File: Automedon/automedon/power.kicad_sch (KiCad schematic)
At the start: 22 parts, among them J29 3211771, J30 3211771, J31 3211771, J32 3211771, J33 3211771, J34 3211771, J35 3211771, J36 3211771, J37 3211771, J38 3211771, J39 3211771, J40 3211771, J41 3211771, J42 3211771, J43 3211771, J44 3211771

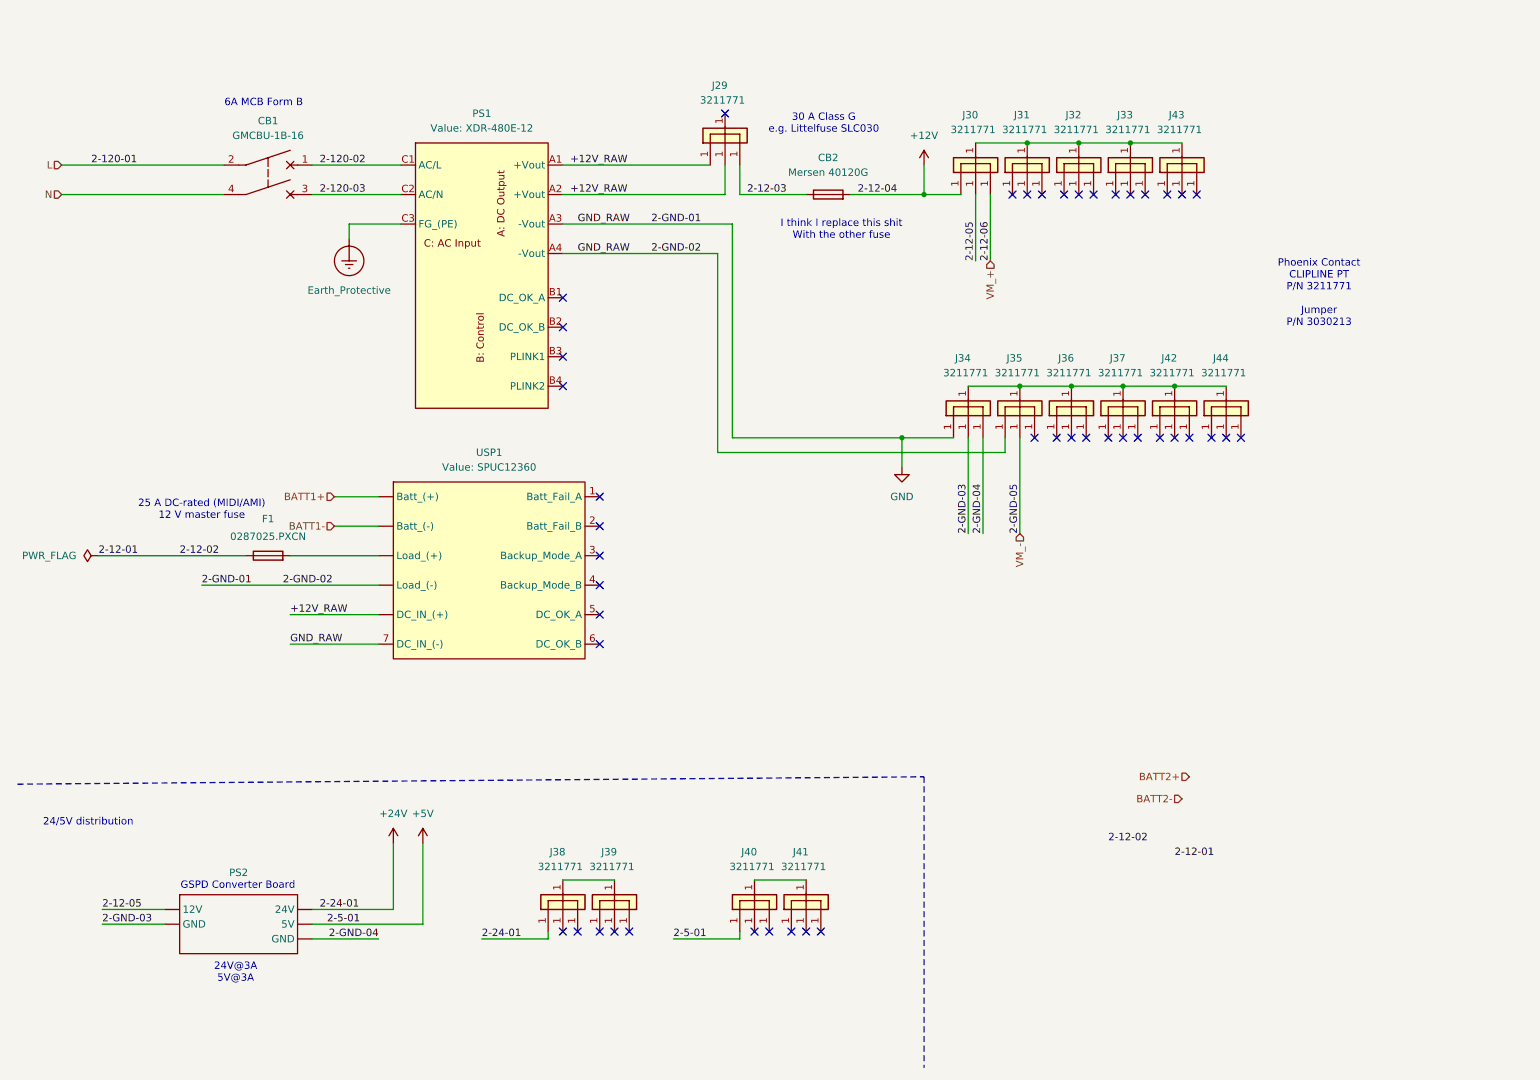
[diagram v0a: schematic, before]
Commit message: Updated schematics and symbols based on feedback
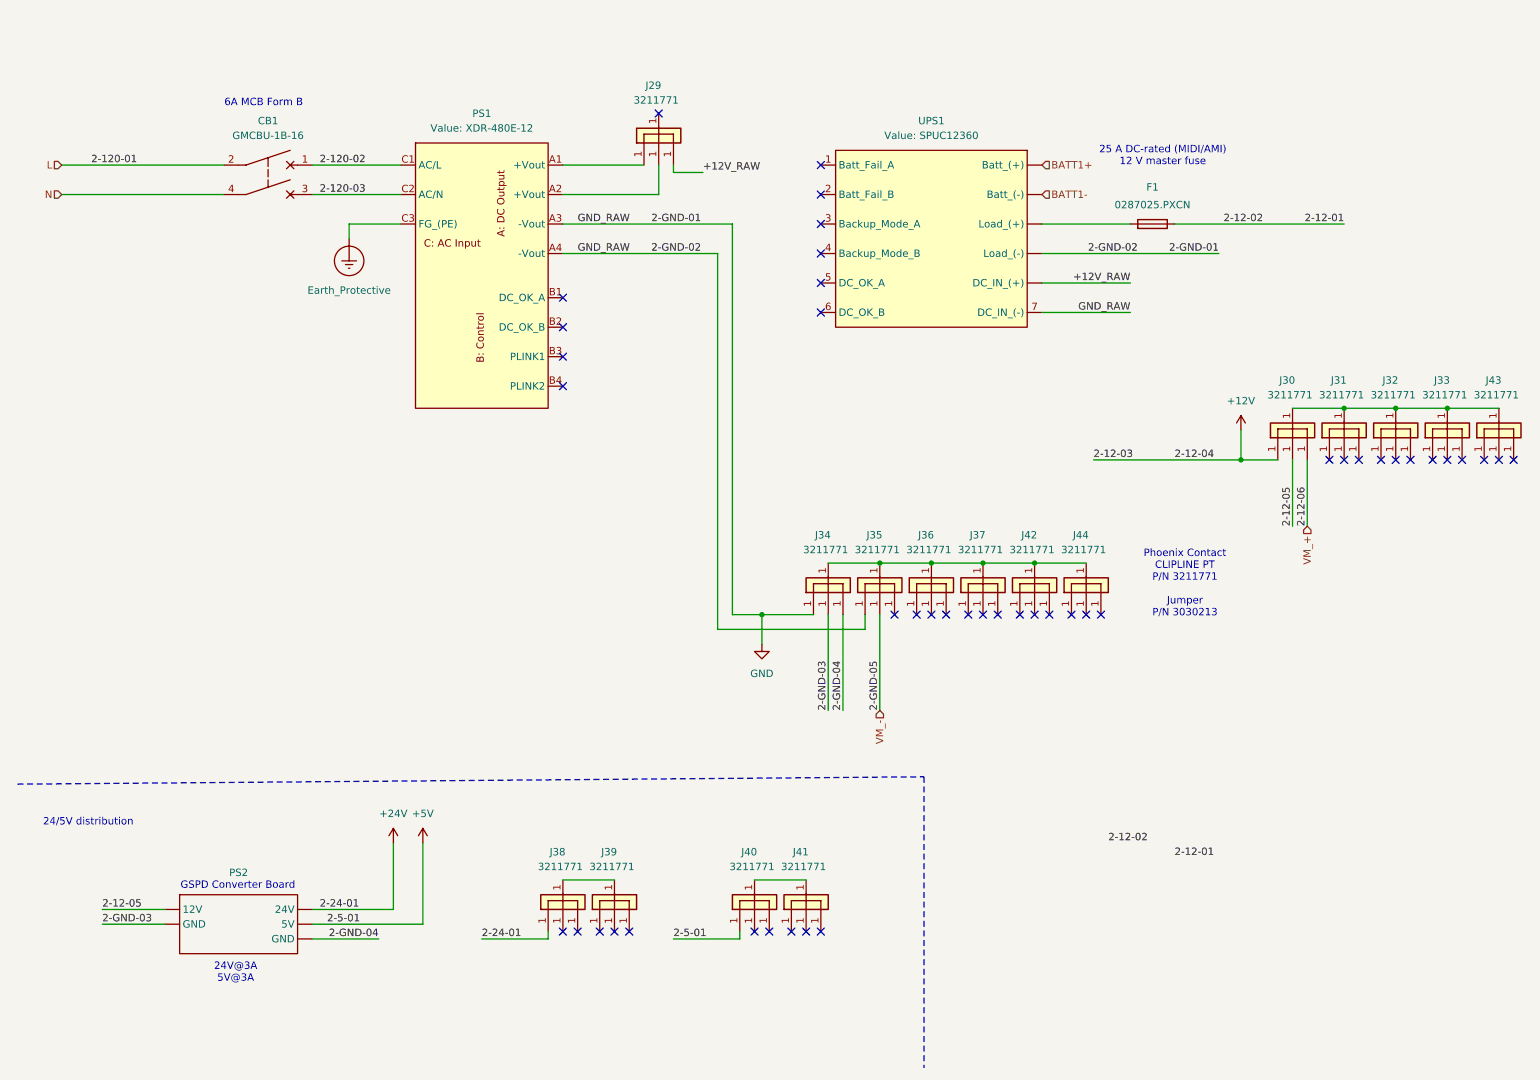
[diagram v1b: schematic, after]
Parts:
- removed CB2: Mersen 40120G, symbol Device:Fuse
- renumbered USP1 to UPS1
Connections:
- net 2-12-03 is gone; now on net +12V_RAW: J29.1
- net +12V_RAW: no longer PS1.A1 (+Vout), PS1.A2 (+Vout)
- net at J37.1: now also J34.1, J35.1, J36.1, J42.1, J44.1
- net at J39.1: no longer J38.1
- net at J41.1: now also J40.1
- new net: J30.1, J31.1, J32.1, J33.1, J43.1
- new net: J29.1, PS1.A1 (+Vout)
- new net: J29.1, PS1.A2 (+Vout)
- new net: J38.1, J39.1
- now unconnected: J31.1, J32.1, J33.1, J36.1, J42.1, J43.1, J44.1
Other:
- note removed: "30 A Class G e.g. Littelfuse SLC030"
- note removed: "I think I replace this shit With the other fuse"
- moved on the sheet: F1, J29, J30, J31, J32, J33, J34, J35, J36, J37, J42, J43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

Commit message: Update power schematic (power.kicad_sch)
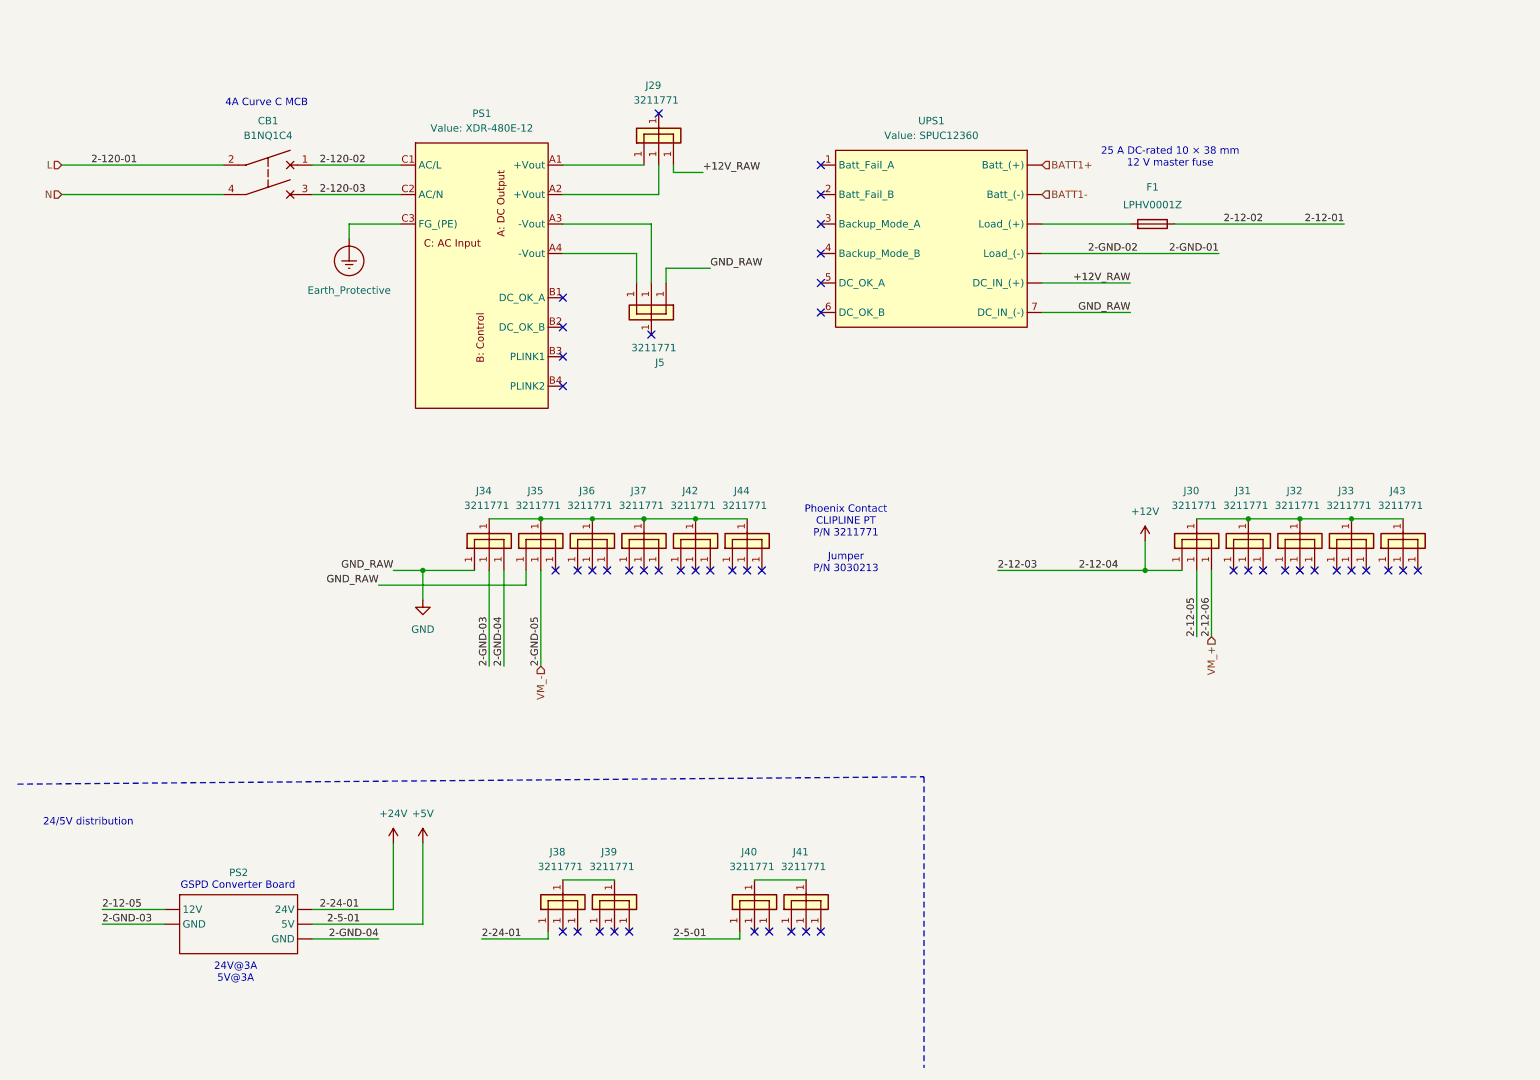
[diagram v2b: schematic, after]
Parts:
- added J5: 3211771, symbol automedon:CONN_TERM_3
- CB1: value GMCBU-1B-16 -> B1NQ1C4
- F1: value 0287025.PXCN -> LPHV0001Z
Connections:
- net GND: now also J5.1; no longer PS1.A3 (-Vout), PS1.A4 (-Vout), UPS1. (DC_IN_(+))
- net at J37.1: now also J34.1, J35.1, J36.1, J42.1, J44.1
- net at J39.1: no longer J38.1
- net at J41.1: now also J40.1
- new net: J30.1, J31.1, J32.1, J33.1, J43.1
- new net: J5.1, PS1.A3 (-Vout)
- new net: J5.1, PS1.A4 (-Vout)
- new net: J38.1, J39.1
- new net 2-GND-01: UPS1. (DC_IN_(+))
- now unconnected: J31.1, J32.1, J33.1, J36.1, J42.1, J43.1, J44.1
- no-connect marks 46 -> 47
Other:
- note added: "25 A DC-rated 10 × 38 mm 12 V master fuse"
- note added: "4A Curve C MCB"
- note removed: "25 A DC-rated (MIDI/AMI) 12 V master fuse"
- note removed: "6A MCB Form B"
- moved on the sheet: J30, J31, J32, J33, J34, J35, J36, J37, J42, J43, J44

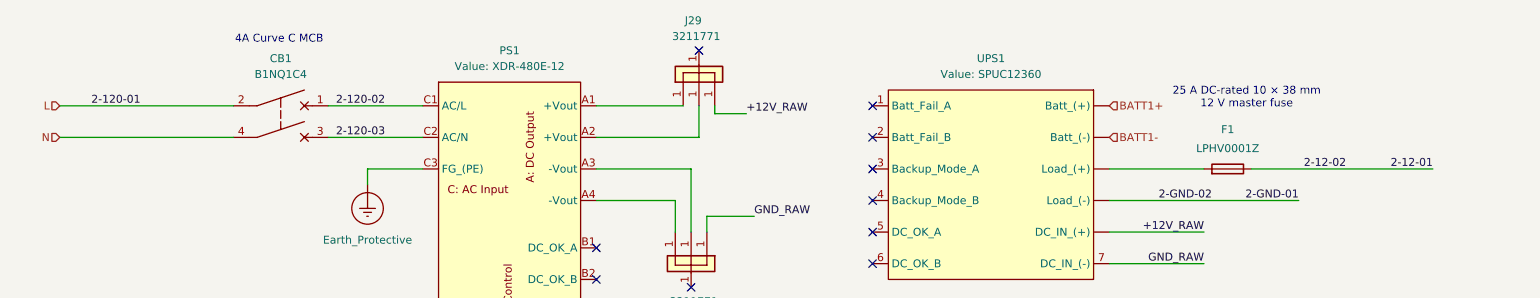
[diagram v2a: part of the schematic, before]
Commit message: updated cb1 and f1 on schematic
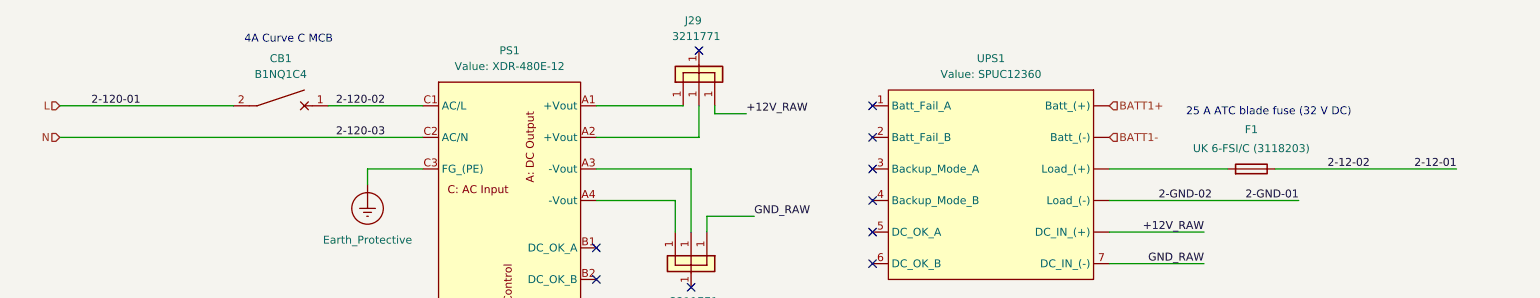
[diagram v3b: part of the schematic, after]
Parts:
- removed CB1: B1NQ1C4, symbol Device:CircuitBreaker_2P
- added CB1: B1NQ1C4, symbol Device:CircuitBreaker_1P
- F1: value LPHV0001Z -> UK 6-FSI/C (3118203)
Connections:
- net 2-120-03 is gone; now on net N: PS1.C2 (AC/N)
- net 2-120-02: now also CB1.1
- net L: now also CB1.2
- net at J37.1: now also J34.1, J35.1, J36.1, J42.1, J44.1
- net at J39.1: no longer J38.1
- net at J41.1: now also J40.1
- new net: J30.1, J31.1, J32.1, J33.1, J43.1
- new net: J38.1, J39.1
- now unconnected: J31.1, J32.1, J33.1, J36.1, J42.1, J43.1, J44.1
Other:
- note added: "25 A ATC blade fuse (32 V DC)"
- note removed: "25 A DC-rated 10 × 38 mm 12 V master fuse"
- moved on the sheet: F1
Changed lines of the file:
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@@
 	(generator_version "9.0")
 	(paper "A4")
-	(text "25 A DC-rated 10 × 38 mm\n12 V master fuse\n"
-		(exclude_from_sim no)
-		(at 211.328 40.64 0)
+	(text "25 A ATC blade fuse (32 V DC)"
+		(exclude_from_sim no)
+		(at 214.884 42.926 0)
 		(effects
 			(font
@@
 	(text "4A Curve C MCB"
 		(exclude_from_sim no)
-		(at 55.626 31.242 0)
+		(at 57.15 31.242 0)
 		(effects
 			(font
@@
 	(wire
 		(pts
-			(xy 20.32 46.99) (xy 48.26 46.99)
+			(xy 20.32 46.99) (xy 78.74 46.99)
 		)
 		(stroke
@@
 	(wire
 		(pts
-			(xy 241.3 52.07) (xy 212.09 52.07)
+			(xy 245.11 52.07) (xy 215.9 52.07)
 		)
 		(stroke
@@
 	(wire
 		(pts
-			(xy 63.5 46.99) (xy 78.74 46.99)
-		)
-		(stroke
-			(width 0)
-			(type default)
-		)
-	)
-	(wire
-		(pts
-			(xy 204.47 52.07) (xy 189.23 52.07)
+			(xy 208.28 52.07) (xy 189.23 52.07)
 		)
 		(stroke
@@
 	)
 	(label "2-12-02"
-		(at 227.33 52.07 180)
+		(at 231.14 52.07 180)
 		(effects
 			(font
@@
 	)
 	(label "2-12-01"
-		(at 241.3 52.07 180)
+		(at 245.11 52.07 180)
 		(effects
 			(font
@@
 	(symbol
 		(lib_id "Device:Fuse")
-		(at 208.28 52.07 270)
+		(at 212.09 52.07 270)
 		(mirror x)
 		(unit 1)
@@
 		(dnp no)
 		(property "Reference" "F1"
-			(at 208.28 45.72 90)
-			(effects
-				(font
-					(size 1.27 1.27)
-				)
-			)
-		)
-		(property "Value" "LPHV0001Z"
-			(at 208.28 48.768 90)
+			(at 212.09 45.72 90)
+			(effects
+				(font
+					(size 1.27 1.27)
+				)
+			)
+		)
+		(property "Value" "UK 6-FSI/C (3118203)"
+			(at 212.09 48.768 90)
 			(effects
 				(font
@@
 		)
 		(property "Footprint" ""
-			(at 208.28 53.848 90)
+			(at 212.09 53.848 90)
 			(effects
 				(font
@@
 		)
 		(property "Datasheet" "~"
-			(at 208.28 52.07 0)
+			(at 212.09 52.07 0)
 			(effects
 				(font
@@
 		)
 		(property "Description" "Fuse"
-			(at 208.28 52.07 0)
+			(at 212.09 52.07 0)
 			(effects
 				(font
@@
 	)
 	(symbol
+		(lib_id "Device:CircuitBreaker_1P")
+		(at 55.88 41.91 270)
+		(unit 1)
+		(exclude_from_sim no)
+		(in_bom yes)
+		(on_board yes)
+		(dnp no)
+		(fields_autoplaced yes)
+		(property "Reference" "CB1"
+			(at 55.88 34.29 90)
+			(effects
+				(font
+					(size 1.27 1.27)
+				)
+			)
+		)
+		(property "Value" "B1NQ1C4"
+			(at 55.88 36.83 90)
+			(effects
+				(font
+					(size 1.27 1.27)
+				)
+			)
+		)
+		(property "Footprint" ""
+			(at 55.88 41.91 0)
+			(effects
+				(font
+					(size 1.27 1.27)
+				)
+				(hide yes)
+			)
+		)
+		(property "Datasheet" "~"
+			(at 55.88 41.91 0)
+			(effects
+				(font
+					(size 1.27 1.27)
+				)
+				(hide yes)
+			)
+		)
+		(property "Description" "Single pole circuit breaker"
+			(at 55.88 41.91 0)
+			(effects
+				(font
+					(size 1.27 1.27)
+				)
+				(hide yes)
+			)
+		)
+		(pin "1"
+		)
+		(pin "2"
+		)
+		(instances
+			(project ""
+				(path "/75831ec5-d9f4-4d6d-a97b-0bb87f785768/71d498b1-1ae2-4b4b-ac1c-08dcfc85d4b3"
+					(reference "CB1")
+					(unit 1)
+				)
+			)
+		)
+	)
+	(symbol
 		(lib_name "CONN_TERM_3_1")
 		(lib_id "automedon:CONN_TERM_3")
@@
 					(unit 1)
 				)
-			)
-		)
-	)
-	(symbol
-		(lib_id "Device:CircuitBreaker_2P")
-		(at 55.88 44.45 270)
-		(unit 1)
-		(exclude_from_sim no)
-		(in_bom yes)
-		(on_board yes)
-		(dnp no)
-		(fields_autoplaced yes)
-		(property "Reference" "CB1"
-			(at 55.88 34.29 90)
-			(effects
-				(font
-					(size 1.27 1.27)
-				)
-			)
-		)
-		(property "Value" "B1NQ1C4"
-			(at 55.88 36.83 90)
-			(effects
-				(font
-					(size 1.27 1.27)
-				)
-			)
-		)
-		(property "Footprint" ""
-			(at 55.88 41.91 0)
-			(effects
-				(font
-					(size 1.27 1.27)
-				)
-				(hide yes)
-			)
-		)
-		(property "Datasheet" "~"
-			(at 55.88 41.91 0)
-			(effects
-				(font
-					(size 1.27 1.27)
-				)
-				(hide yes)
-			)
-		)
-		(property "Description" "Double pole circuit breaker"
-			(at 55.88 44.45 0)
-			(effects
-				(font
-					(size 1.27 1.27)
-				)
-				(hide yes)
-			)
-		)
-		(pin "4"
-		)
-		(pin "1"
-		)
-		(pin "2"
-		)
-		(pin "3"
-		)
-		(instances
-			(project "automedon"
-				(path "/75831ec5-d9f4-4d6d-a97b-0bb87f785768/71d498b1-1ae2-4b4b-ac1c-08dcfc85d4b3"
-					(reference "CB1")
-					(unit 1)
-				)

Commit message: Minor power path changes
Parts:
- added J46, J47, J48, J49, J6: 3211771, symbol automedon:CONN_TERM_3
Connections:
- net 2-GND-01 is gone; now on net GND: UPS1. (DC_IN_(+))
- net +12V: now also F1.1
- net 2-12-01: now also F1.2, UPS1. (DC_IN_(+)); no longer F1.1
- net GND: no longer J35.1, J5.1, UPS1.7 (DC_IN_(-))
- net at J37.1: now also J34.1, J35.1, J36.1, J42.1, J44.1, J46.1, J47.1, J48.1, J49.1
- net GND_RAW: now reaches J5.1
- net GND_RAW: now also UPS1.7 (DC_IN_(-))
- net at J39.1: no longer J38.1
- net at J41.1: now also J40.1
- new net: J30.1, J31.1, J32.1, J33.1, J43.1
- new net: J38.1, J39.1, J6.1
- now unconnected: J31.1, J32.1, J33.1, J36.1, J42.1, J43.1, J44.1
- no-connect marks 47 -> 62
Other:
- note added: "12V BUS"
- note added: "24V BUS"
- note added: "GND BUS"
- moved on the sheet: F1, J30, J31, J32, J33, J34, J35, J36, J37, J40, J41, J42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
